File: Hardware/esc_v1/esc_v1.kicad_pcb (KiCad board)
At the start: 4 copper layers, 127 parts, among them J1 vcc_connector, J2 SWD_tag_connect, J3 motor_connector, J4 10118193-0001LF, Q1 IRFH7084TRPBF, Q2 IRFH7084TRPBF, Q3 IRFH7084TRPBF, Q4 IRFH7084TRPBF, Q5 IRFH7084TRPBF, Q6 IRFH7084TRPBF, SW1 SW_Push, U1 AZ1117CH-5.0TRG1, U10 MAX40056UAUA/V+, U2 AZ1117CH-3.3TRG1, U3 TPS5450DDAR, U4 ATSAME70J21A-AN, U5 CP2102N-Axx-xQFN24, U6 UCC27282DR, U7 UCC27282DR, U8 UCC27282DR, U9 MAX40056UAUA/V+, Y1 Crystal_GND2

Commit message: Fixing footprints
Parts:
- Q1, Q2, Q3, Q4, Q5, Q6: footprint IRFH7084PbF:IRFH7084TRPBF -> IRFH7084PbF:Infineon-PQFN5x6-G-02_2017-22-MFG
- moved Q1 56.5 mm to (207.9, 110.3)
- moved Q3 53.1 mm to (201.5, 100.6)
- moved Q6 48.5 mm to (207.9, 100.6)
- moved Q4 42.1 mm to (201.5, 110.3)
- moved Q5 38.5 mm to (183.1, 88.4)
- moved Q2 34.6 mm to (195.1, 100.6)
- moved D1 21.2 mm to (147.0, 113.5), turned to 90 degrees
- moved D4 18.0 mm to (144.0, 113.5), turned to 90 degrees
- moved R26 17.1 mm to (145.0, 113.5), turned to -90 degrees
- moved D5 15.8 mm to (141.0, 113.5), turned to 90 degrees
- moved C35 14.8 mm to (126.0, 96.0), turned to 0 degrees
- moved D13 13.8 mm to (132.0, 95.0), turned to 180 degrees
- moved C34 13.3 mm to (121.0, 103.0)
- moved C36 12.1 mm to (126.0, 94.0), turned to 0 degrees
- moved U6 11.7 mm to (125.0, 101.0)
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
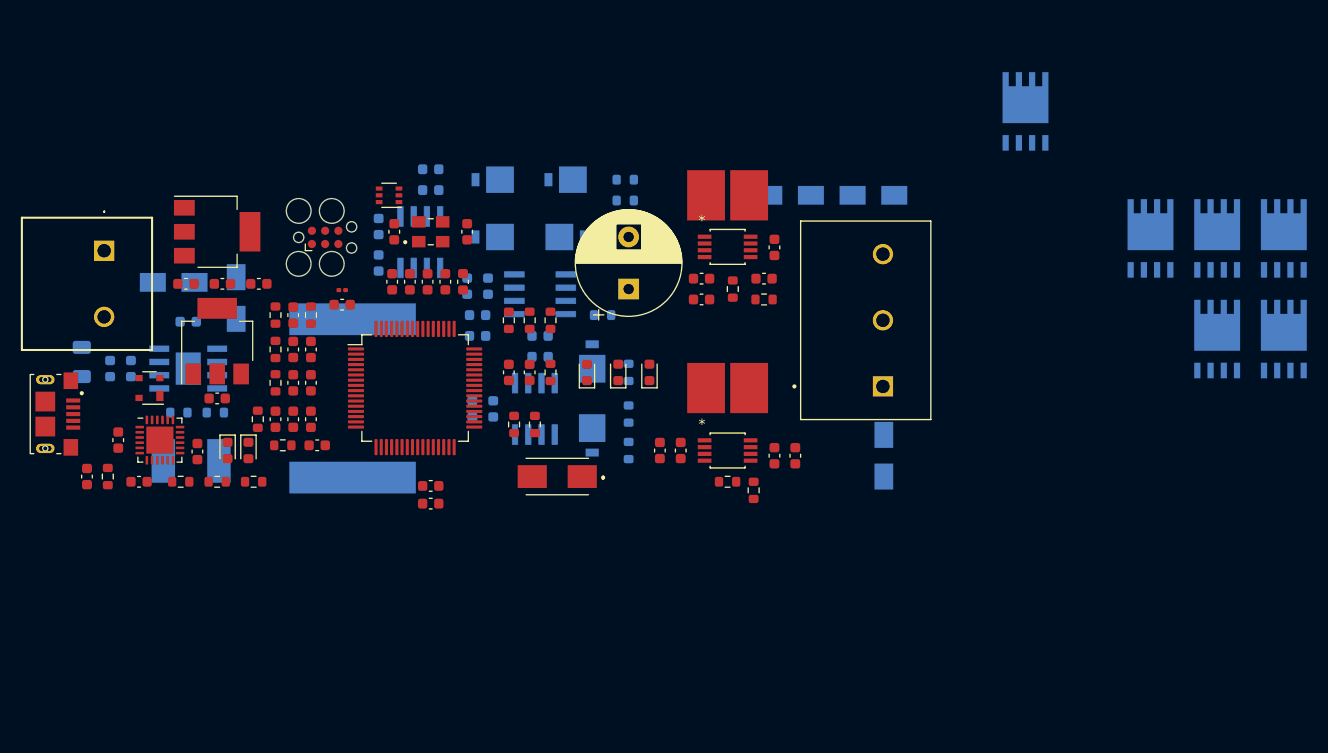
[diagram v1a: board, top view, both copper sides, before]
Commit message: changed gate driver, removed 10V buck and 5V LDO, added 5V buck. Started on Layout
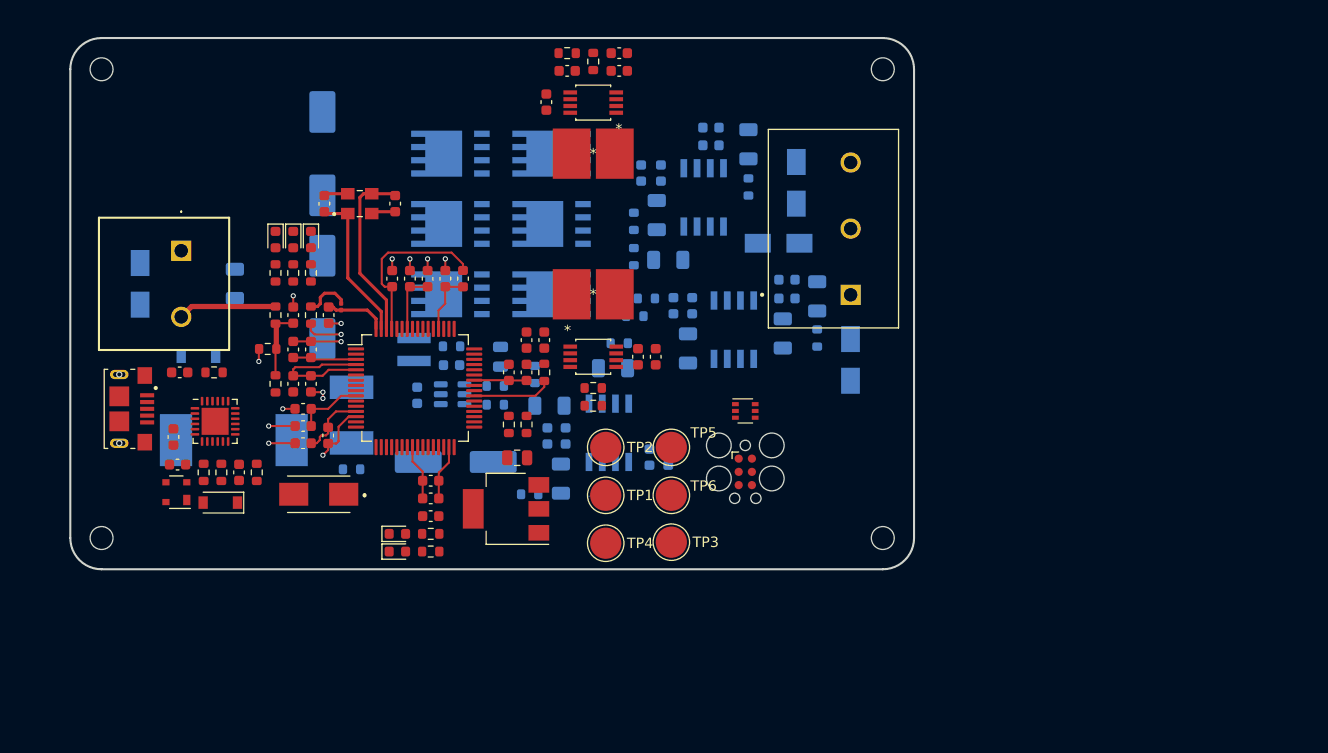
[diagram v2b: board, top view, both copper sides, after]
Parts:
- removed D11, D12: LED orange, LED_SMD:LED_0603_1608Metric
- removed R20, R21: 330R, Resistor_SMD:R_0603_1608Metric
- removed U7, U8: UCC27282DR, UCC27282DR:SOIC127P599X175-8N
- added D19: D_Schottky, Diode_SMD:D_1206_3216Metric, B.Cu at (156.5, 91.6)
- added D20: D_Schottky, Diode_SMD:D_1206_3216Metric, B.Cu at (148.8, 102.7)
- added D21: D_Schottky, Diode_SMD:D_1206_3216Metric, B.Cu at (147.7, 98.4)
- added D22: LED green, LED_SMD:LED_0603_1608Metric, F.Cu at (122.8, 129.0)
- added D23: D_Schottky, Diode_SMD:D_SOD-123, F.Cu at (105.8, 126.0)
- added D24: D_Schottky, Diode_SMD:D_SOD-123, B.Cu at (103.7, 112.0)
- added H1: MountingHole, MountingHole:MountingHole_2.2mm_M2, F.Cu at (94.4, 84.4)
- added H2: MountingHole, MountingHole:MountingHole_2.2mm_M2, F.Cu at (169.4, 129.4)
- added H3: MountingHole, MountingHole:MountingHole_2.2mm_M2, F.Cu at (94.4, 129.4)
- added H4: MountingHole, MountingHole:MountingHole_2.2mm_M2, F.Cu at (169.4, 84.4)
- added IC1: RT8259GE, Package_TO_SOT_SMD:SOT-23-6, B.Cu at (128.1, 115.6)
- added L3: 47uH, SRP1265A-470M:SRP1265A, B.Cu at (107.1, 120.0)
- added R12: 1K, Resistor_SMD:R_0603_1608Metric, F.Cu at (126.0, 129.0)
- added R34: 10R, Resistor_SMD:R_0603_1608Metric, B.Cu at (146.7, 106.4)
- added R35: 0R, Resistor_SMD:R_0603_1608Metric, B.Cu at (156.5, 95.7)
- added R36: 10R, Resistor_SMD:R_0603_1608Metric, B.Cu at (145.5, 102.4)
- added R37: 10R, Resistor_SMD:R_0603_1608Metric, B.Cu at (145.5, 99.0)
- added R5: 62K, Resistor_SMD:R_0603_1608Metric, B.Cu at (132.2, 114.8)
- added R6: 11.8K, Resistor_SMD:R_0603_1608Metric, B.Cu at (132.2, 116.6)
- added TP1: TestPoint, TestPoint:TestPoint_Pad_D3.0mm, F.Cu at (142.8, 125.3)
- added TP2: TestPoint, TestPoint:TestPoint_Pad_D3.0mm, F.Cu at (142.8, 120.7)
- added TP3: TestPoint, TestPoint:TestPoint_Pad_D3.0mm, F.Cu at (149.1, 129.8)
- added TP4: TestPoint, TestPoint:TestPoint_Pad_D3.0mm, F.Cu at (142.8, 129.9)
- added TP5: TestPoint, TestPoint:TestPoint_Pad_D3.0mm, F.Cu at (149.1, 120.7)
- added TP6: TestPoint, TestPoint:TestPoint_Pad_D3.0mm, F.Cu at (149.1, 125.3)
- C10: value 150uF, 50mOhm -> 1uF; footprint T510E107M025ATE050:T510E107M025AT E050 -> Capacitor_SMD:C_0603_1608Metric
- C2: moved to B.Cu
- C33, C37: value 1uF -> 1000pF
- C34, C38, C44: value 1000pF -> 100nF
- C35, C39: value 100nF -> 1uF
- C36, C42: value 1000pF -> 1uF
- C4: value 22uF -> 10nF
- C40: value 1000pF -> 270uF; footprint Capacitor_SMD:C_0603_1608Metric -> Capacitor_SMD:CP_Elec_10x10
- C41: value 1uF -> 270uF; footprint Capacitor_SMD:C_0603_1608Metric -> Capacitor_SMD:CP_Elec_10x10
- C43: value 100nF -> 1000pF
- C45: value 1000uF -> 1uF; footprint Capacitor_THT:CP_Radial_D10.0mm_P5.00mm -> Capacitor_SMD:C_0603_1608Metric; moved to B.Cu
- C5: value 22uF -> 100uF; footprint Capacitor_SMD:C_0603_1608Metric -> T510E107M025ATE050:T510E107M025AT E050
- C6: footprint Capacitor_SMD:C_0603_1608Metric -> Capacitor_SMD:C_0805_2012Metric; moved to B.Cu
- C7: footprint Capacitor_SMD:C_0603_1608Metric -> Capacitor_SMD:C_0805_2012Metric
- C8: value 10nF -> 390uF, 20mOhm; footprint Capacitor_SMD:C_0603_1608Metric -> Capacitor_SMD:C_Elec_8x10.2
- D10: value Schottky, 0.5V 3A -> LED green; footprint Diode_SMD:D_SMA -> LED_SMD:LED_0603_1608Metric; moved to F.Cu
- D13, D14, D15, D16, D17, D18: footprint SS2P4-M3_84A:SS2P4M384A -> Diode_SMD:D_1206_3216Metric
- L1: value 15uH, 14.4mOhm -> 10uH; footprint IHLP6767GZER150M11:INDPM172172X700N -> 744025100:Wuerth_Elektronik-744025100-Manufacturer_Recommended
- R1, R2, R3: value 330R -> 1K
- R10: value 10K -> 1K; moved to F.Cu
- R11: value 1.4K -> 0R
- R23, R26: value 1R -> 0R
- R24, R25, R27: value 1R -> 10R
- U1: value AZ1117CH-5.0TRG1 -> FAN7390MX; footprint Package_TO_SOT_SMD:SOT-223-3_TabPin2 -> FAN7390MX:Fairchild-CASE_751EG-0-0-0; moved to B.Cu
- U3: value TPS5450DDAR -> FAN7390MX; footprint Package_SO:TI_SO-PowerPAD-8 -> FAN7390MX:Fairchild-CASE_751EG-0-0-0
- U6: value UCC27282DR -> FAN7390MX; footprint UCC27282DR:SOIC127P599X175-8N -> FAN7390MX:Fairchild-CASE_751EG-0-0-0
- moved Q1 82.0 mm to (127.9, 92.5), turned to -90 degrees
- moved Q3 73.8 mm to (127.9, 106.0), turned to -90 degrees
- moved Q6 70.3 mm to (137.6, 99.2), turned to -90 degrees
- moved Q4 64.0 mm to (137.6, 106.0), turned to -90 degrees
- moved Q2 58.1 mm to (137.6, 92.5), turned to -90 degrees
- moved Q5 56.3 mm to (127.9, 99.2), turned to -90 degrees
- moved U3 52.5 mm to (155.1, 109.4)
- moved J2 46.2 mm to (156.2, 123.0), turned to -90 degrees
- moved C10 45.8 mm to (148.8, 121.6), turned to 90 degrees
- moved D2 40.0 mm to (156.2, 117.2), turned to 0 degrees
- moved U1 38.6 mm to (143.1, 119.3), turned to 0 degrees
- moved U2 38.4 mm to (133.2, 126.6), turned to 180 degrees
- moved R22 38.3 mm to (118.4, 122.8)
- moved D1 38.1 mm to (111.1, 100.8), turned to -90 degrees
- moved C33 34.1 mm to (147.0, 121.6)
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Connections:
- net Net-(C1-Pad1) renamed /shield
- net Net-(C48-Pad1) renamed /Powerstage/measurements_phase_U/Ref
- net Net-(C52-Pad1) renamed /Powerstage/measurements_phase_V/Ref
- C10 pad 1: +10V -> /+BATT_filtered
- C2 pad 1: +10V -> /+BATT_filtered
- C33 pad 1: +10V -> /+BATT_filtered
- C34 pad 1: +10V -> /Powerstage/Gate_driver_V/Bootstrap+
- C34 pad 2: GND -> /Powerstage/Gate_driver_V/HS
- C35 pad 1: /Powerstage/Gate_driver_phase_U/GD_HB -> /Powerstage/Gate_driver_V/Bootstrap+
- C35 pad 2: /Powerstage/Gate_driver_phase_U/HS -> /Powerstage/Gate_driver_V/HS
- C36 pad 1: /Powerstage/Gate_driver_phase_U/GD_HB -> /+BATT_filtered
- C36 pad 2: /Powerstage/Gate_driver_phase_U/HS -> GND
- C37 pad 1: +10V -> /+BATT_filtered
- C38 pad 1: +10V -> /Powerstage/Gate_driver_W/Bootstrap+
- C38 pad 2: GND -> /PHASE_W
- C39 pad 1: /Powerstage/Gate_driver_phase_V/GD_HB -> /Powerstage/Gate_driver_W/Bootstrap+
- C39 pad 2: /Powerstage/Gate_driver_phase_V/HS -> /PHASE_W
- C4 pad 1: VCC -> Net-(C4-Pad1)
- C4 pad 2: GND -> Net-(C4-Pad2)
- C40 pad 1: /Powerstage/Gate_driver_phase_V/GD_HB -> Net-(C40-Pad1)
- C40 pad 2: /Powerstage/Gate_driver_phase_V/HS -> GND
- C41 pad 1: +10V -> Net-(C40-Pad1)
- C42 pad 1: +10V -> /+BATT_filtered
- C43 pad 1: /Powerstage/Gate_driver_phase_W/GD_HB -> /+BATT_filtered
- C43 pad 2: /PHASE_W -> GND
- C44 pad 1: /Powerstage/Gate_driver_phase_W/GD_HB -> /Powerstage/Gate_driver_U/Bootstrap+
- C44 pad 2: /PHASE_W -> /Powerstage/Gate_driver_U/HS
- C45 pad 1: +BATT -> /Powerstage/Gate_driver_U/Bootstrap+
- C45 pad 2: GND -> /Powerstage/Gate_driver_U/HS
- C5 pad 1: VCC -> /+BATT_filtered
- C8 pad 2: Net-(C8-Pad2) -> GND
- D10 pad 1: Net-(C8-Pad2) -> GND
- D10 pad 2: GND -> Net-(D10-Pad2)
- D13 pad 1: /Powerstage/Gate_driver_phase_U/GD_HS -> /Powerstage/Gate_driver_V/Bootstrap+
- D13 pad 2: /Powerstage/Gate_driver_phase_U/HS -> Net-(D13-Pad2)
- D14 pad 1: /Powerstage/Gate_driver_phase_U/GD_LO -> /Powerstage/Gate_driver_V/GD_HO
- D14 pad 2: GND -> /Powerstage/Gate_driver_V/HS
- D15 pad 1: /Powerstage/Gate_driver_phase_V/GD_HS -> /Powerstage/Gate_driver_V/GD_LO
- D15 pad 2: /Powerstage/Gate_driver_phase_V/HS -> GND
- D16 pad 1: /Powerstage/Gate_driver_phase_V/GD_LO -> /Powerstage/Gate_driver_W/Bootstrap+
- D16 pad 2: GND -> Net-(D16-Pad2)
- D17 pad 1: /Powerstage/Gate_driver_phase_W/GD_HS -> /Powerstage/Gate_driver_W/GD_HO
- D18 pad 1: /Powerstage/Gate_driver_phase_W/GD_LO -> /Powerstage/Gate_driver_W/GD_LO
- F1 pad 2: VCC -> Net-(C40-Pad1)
- J4 pad 1: +5V -> /VBUS
- L1 pad 1: Net-(C8-Pad2) -> Net-(C4-Pad2)
- L1 pad 2: +10V -> Net-(L1-Pad2)
- Q1 pad 1: /Powerstage/Gate_driver_phase_U/HS -> /Powerstage/Gate_driver_U/HS
- Q1 pad 2: /Powerstage/Gate_driver_phase_U/HS -> /Powerstage/Gate_driver_U/HS
- Q1 pad 3: /Powerstage/Gate_driver_phase_U/HS -> /Powerstage/Gate_driver_U/HS
- Q1 pad 4: /Powerstage/Gate_driver_phase_U/HO -> /Powerstage/Gate_driver_U/HO
- Q1 pad 5-6-7-8: +BATT -> Net-(C40-Pad1)
- Q2 pad 4: /Powerstage/Gate_driver_phase_U/LO -> /Powerstage/Gate_driver_U/LO
- Q2 pad 5-6-7-8: /Powerstage/Gate_driver_phase_U/HS -> /Powerstage/Gate_driver_U/HS
- Q3 pad 1: /Powerstage/Gate_driver_phase_V/HS -> /Powerstage/Gate_driver_V/HS
- Q3 pad 2: /Powerstage/Gate_driver_phase_V/HS -> /Powerstage/Gate_driver_V/HS
- Q3 pad 3: /Powerstage/Gate_driver_phase_V/HS -> /Powerstage/Gate_driver_V/HS
- Q3 pad 4: /Powerstage/Gate_driver_phase_V/HO -> /Powerstage/Gate_driver_V/HO
- Q3 pad 5-6-7-8: +BATT -> Net-(C40-Pad1)
- Q4 pad 4: /Powerstage/Gate_driver_phase_V/LO -> /Powerstage/Gate_driver_V/LO
- Q4 pad 5-6-7-8: /Powerstage/Gate_driver_phase_V/HS -> /Powerstage/Gate_driver_V/HS
- Q5 pad 4: /Powerstage/Gate_driver_phase_W/HO -> /Powerstage/Gate_driver_W/HO
- Q5 pad 5-6-7-8: +BATT -> Net-(C40-Pad1)
- Q6 pad 4: /Powerstage/Gate_driver_phase_W/LO -> /Powerstage/Gate_driver_W/LO
- R10 pad 1: +10V -> +3V3
- R10 pad 2: Net-(R10-Pad2) -> Net-(D10-Pad2)
- R11 pad 1: Net-(R10-Pad2) -> Net-(L1-Pad2)
- R11 pad 2: GND -> +5V
- R22 pad 1: /Powerstage/Gate_driver_phase_U/GD_HS -> /+BATT_filtered
- R22 pad 2: /Powerstage/Gate_driver_phase_U/HO -> Net-(C8-Pad1)
- R23 pad 1: /Powerstage/Gate_driver_phase_U/GD_LO -> Net-(D13-Pad2)
- R23 pad 2: /Powerstage/Gate_driver_phase_U/LO -> /+BATT_filtered
- R24 pad 1: /Powerstage/Gate_driver_phase_V/GD_HS -> /Powerstage/Gate_driver_V/HO
- R24 pad 2: /Powerstage/Gate_driver_phase_V/HO -> /Powerstage/Gate_driver_V/GD_HO
- R25 pad 1: /Powerstage/Gate_driver_phase_V/GD_LO -> /Powerstage/Gate_driver_V/LO
- R25 pad 2: /Powerstage/Gate_driver_phase_V/LO -> /Powerstage/Gate_driver_V/GD_LO
- R26 pad 1: /Powerstage/Gate_driver_phase_W/GD_HS -> Net-(D16-Pad2)
- R26 pad 2: /Powerstage/Gate_driver_phase_W/HO -> /+BATT_filtered
- R27 pad 1: /Powerstage/Gate_driver_phase_W/GD_LO -> /Powerstage/Gate_driver_W/HO
- R27 pad 2: /Powerstage/Gate_driver_phase_W/LO -> /Powerstage/Gate_driver_W/GD_HO
- R28 pad 1: /Powerstage/Gate_driver_phase_U/HS -> /Powerstage/Gate_driver_U/HS
- R31 pad 1: /Powerstage/Gate_driver_phase_V/HS -> /Powerstage/Gate_driver_V/HS
- R7 pad 1: VCC -> +BATT
- U1 pad 1: GND -> /MCU/PWM_H1
- U1 pad 2: +5V -> /MCU/PWM_L1
- U1 pad 3: +10V -> GND
- U10 pad 1: /Powerstage/Gate_driver_phase_V/HS -> /Powerstage/Gate_driver_V/HS
- U3 pad 1: Net-(C8-Pad1) -> /MCU/PWM_H2
- U3 pad 2: unconnected-(U3-Pad2) -> /MCU/PWM_L2
- U3 pad 3: unconnected-(U3-Pad3) -> GND
- U3 pad 4: Net-(R10-Pad2) -> /Powerstage/Gate_driver_W/GD_LO
- U3 pad 5: unconnected-(U3-Pad5) -> /+BATT_filtered
- U3 pad 6: GND -> /PHASE_W
- U3 pad 7: VCC -> /Powerstage/Gate_driver_W/GD_HO
- U3 pad 8: Net-(C8-Pad2) -> /Powerstage/Gate_driver_W/Bootstrap+
- U5 pad 13: Net-(D12-Pad1) -> unconnected-(U5-Pad13)
- U5 pad 14: Net-(D11-Pad1) -> unconnected-(U5-Pad14)
- U6 pad 1: +10V -> /MCU/PWM_H0
- U6 pad 2: /Powerstage/Gate_driver_phase_U/GD_HB -> /MCU/PWM_L0
- U6 pad 3: /Powerstage/Gate_driver_phase_U/GD_HS -> GND
- U6 pad 4: /Powerstage/Gate_driver_phase_U/HS -> /Powerstage/Gate_driver_U/GD_LO
- U6 pad 5: /MCU/PWM_H0 -> /+BATT_filtered
- U6 pad 6: /MCU/PWM_L0 -> /Powerstage/Gate_driver_U/HS
- U6 pad 7: GND -> /Powerstage/Gate_driver_U/GD_HO
- U6 pad 8: /Powerstage/Gate_driver_phase_U/GD_LO -> /Powerstage/Gate_driver_U/Bootstrap+
- U9 pad 1: /Powerstage/Gate_driver_phase_U/HS -> /Powerstage/Gate_driver_U/HS
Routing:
- net GND: track 0.00 -> 36.4 mm, vias 0 -> 14
- net /MCU/VDDCORE: track 0.00 -> 34.7 mm
- net +3V3: track 0.00 -> 34.2 mm, vias 0 -> 1
- net /MCU/XOUT: track 0.00 -> 17.6 mm
- net /MCU/XIN: track 0.00 -> 14.7 mm
- net +BATT: track 0.00 -> 9.46 mm
- net /SWCLK: track 0.00 -> 7.65 mm
- net Net-(C9-Pad1): track 0.00 -> 6.73 mm
- net /MCU/VDDPLL: track 0.00 -> 6.02 mm
- net /MCU/VDDPLLUSB: track 0.00 -> 5.99 mm
- net Net-(L2-Pad1): track 0.00 -> 4.41 mm
- net /PHASE_W: track 0.00 -> 0.78 mm
- net /Powerstage/Gate_driver_V/GD_HO: track 0.00 -> 0.55 mm
- added copper zone on In1.Cu, net +3V3
- added copper zone on In2.Cu, net GND
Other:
- board outline added: 81 x 51 mm

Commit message: Continued on layout
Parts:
- moved H2 35.5 mm to (119.9, 140.8)
- moved H0 34.3 mm to (112.7, 141.7)
- moved L0 34.3 mm to (112.7, 137.1)
- moved L1 34.3 mm to (112.7, 146.2)
- moved H1 34.3 mm to (119.0, 146.2)
- moved L2 27.3 mm to (126.4, 140.4)
- moved D10 22.1 mm to (144.8, 128.2), turned to 90 degrees
- moved R30 20.5 mm to (122.8, 91.9), turned to 90 degrees
- moved R29 20.4 mm to (122.8, 95.2), turned to 90 degrees
- moved D22 20.0 mm to (142.8, 128.2), turned to 90 degrees
- moved R10 19.6 mm to (144.8, 125.0), turned to -90 degrees
- moved C46 17.8 mm to (128.8, 91.9), turned to -90 degrees
- moved C48 17.5 mm to (125.8, 96.0)
- moved R12 17.2 mm to (142.8, 125.0), turned to -90 degrees
- moved U9 16.3 mm to (125.9, 91.9), turned to -90 degrees
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- renumbered TP1 to H0, TP3 to H1, TP5 to H2, TP2 to L0, TP4 to L1, TP6 to L2
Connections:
- D9 pad 2: +5V -> /VBUS
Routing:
- net GND: track 36.4 -> 125.0 mm, vias 14 -> 35
- net +5V: track 0.00 -> 80.2 mm, vias 0 -> 2
- net /+BATT_filtered: track 0.00 -> 50.4 mm
- net +3V3: track 34.2 -> 75.9 mm, vias 1 -> 14
- net /NRST: track 0.00 -> 41.2 mm, vias 0 -> 2
- net /MCU/LED_2: track 0.00 -> 36.5 mm, vias 0 -> 2
- net /MCU/LED_1: track 0.00 -> 34.6 mm, vias 0 -> 2
- net /Powerstage/Gate_driver_W/GD_HO: track 0.00 -> 33.7 mm
- net /TRACESWO: track 0.00 -> 33.5 mm, vias 0 -> 3
- net /MCU/LED_0: track 0.00 -> 32.7 mm, vias 0 -> 2
- net /SWDIO: track 0.11 -> 32.1 mm
- net /Powerstage/Gate_driver_U/HS: track 0.00 -> 31.8 mm, vias 0 -> 6
- net /PHASE_W: track 0.78 -> 25.8 mm, vias 0 -> 6
- net /SWCLK: track 7.65 -> 30.7 mm
- net /MCU/UART0_TX: track 0.00 -> 21.3 mm
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- added copper zone on F.Cu, net +3V3
- added copper zone on In1.Cu, net +5V
- added copper zone on B.Cu, net +BATT
- added copper zone on F.Cu, net /PHASE_U
- added copper zone on F.Cu, net /PHASE_V
- added copper zone on B.Cu, net /PHASE_W
- added copper zone on F.Cu, net /PHASE_W
- added copper zone on B.Cu, net /Powerstage/Gate_driver_U/HS
- added copper zone on F.Cu, net /Powerstage/Gate_driver_U/HS
- added copper zone on B.Cu, net /Powerstage/Gate_driver_V/HS
- added copper zone on F.Cu, net /Powerstage/Gate_driver_V/HS
- added copper zone on B.Cu, net GND
- added copper zone on B.Cu, net Net-(C40-Pad1)
- added copper zone on B.Cu, net Net-(D24-Pad1)
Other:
- board size 81 x 51 mm -> 81 x 45 mm

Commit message: Continued on layout
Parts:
- H0, H1, H2, L0, L1, L2: footprint TestPoint:TestPoint_Pad_D3.0mm -> TestPoint:TestPoint_Pad_D2.0mm
- moved H0 57.2 mm to (153.9, 102.1), turned to 180 degrees
- moved L0 51.6 mm to (150.6, 102.0), turned to 180 degrees
- moved H2 41.2 mm to (151.7, 114.6)
- moved L1 37.1 mm to (138.2, 119.3)
- moved L2 33.8 mm to (148.3, 114.7)
- moved H1 33.1 mm to (141.1, 121.6)
- moved C2 10.9 mm to (125.1, 126.4), turned to -90 degrees
- moved R6 9.65 mm to (131.9, 126.2), turned to -90 degrees
- moved R22 9.19 mm to (122.7, 114.7), turned to 90 degrees
- moved R5 9.04 mm to (131.9, 123.1)
- moved R11 8.89 mm to (131.6, 120.0)
- moved C4 8.86 mm to (128.6, 121.7)
- moved C6 8.86 mm to (133.9, 122.7)
- moved IC1 8.86 mm to (128.6, 124.5)
- moved L1 8.65 mm to (124.1, 121.1)
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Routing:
- net /MCU/PWM_L2: track 0.00 -> 44.9 mm, vias 0 -> 3
- net /MCU/PWM_H2: track 0.00 -> 35.2 mm, vias 0 -> 3
- net +5V: track 80.2 -> 50.7 mm, vias 2 -> 4
- net /+BATT_filtered: track 50.4 -> 79.8 mm, vias 0 -> 1
- net /MCU/PWM_H1: track 0.00 -> 26.8 mm, vias 0 -> 3
- net /Powerstage/Gate_driver_U/HO: track 0.00 -> 21.8 mm, vias 0 -> 2
- net /MCU/PWM_L1: track 0.00 -> 20.6 mm, vias 0 -> 3
- net /Powerstage/Gate_driver_W/HO: track 0.00 -> 20.1 mm, vias 0 -> 2
- net Net-(L1-Pad2): track 2.13 -> 9.89 mm
- net /Powerstage/Gate_driver_W/GD_HO: track 33.7 -> 28.8 mm
- net /SWDIO: track 32.1 -> 35.4 mm
- net Net-(D13-Pad2): track 2.22 -> 0.01 mm
- net Net-(C8-Pad1): track 5.86 -> 3.89 mm
- net GND: track 125.0 -> 123.8 mm
- net /MCU/LED_2: track 36.5 -> 37.7 mm
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- added copper zone on B.Cu, net +5V
- added copper zone on F.Cu, net +5V
- added copper zone on B.Cu, net /+BATT_filtered
- removed copper zone on In1.Cu, net +5V

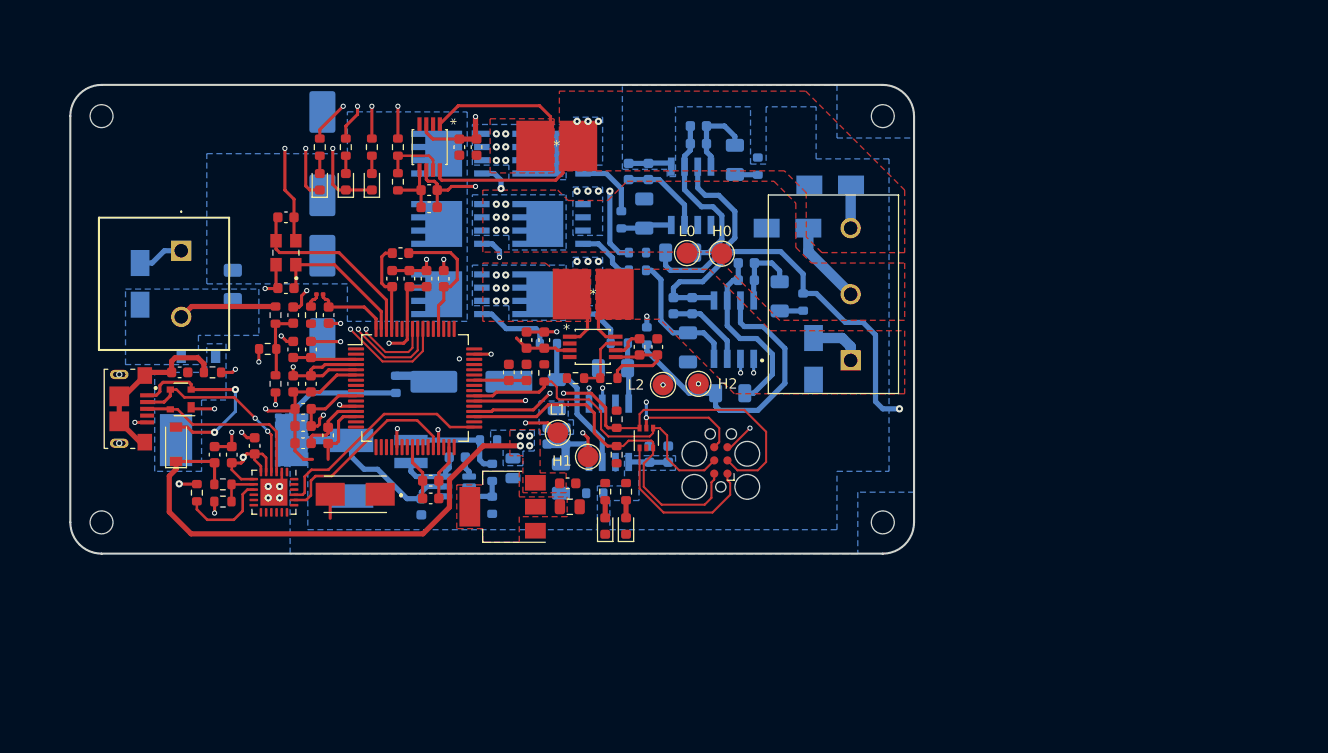
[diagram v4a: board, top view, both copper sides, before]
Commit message: Changed to 6 layer pcb, increased space by 10mm, redid gate driver traces and power planes
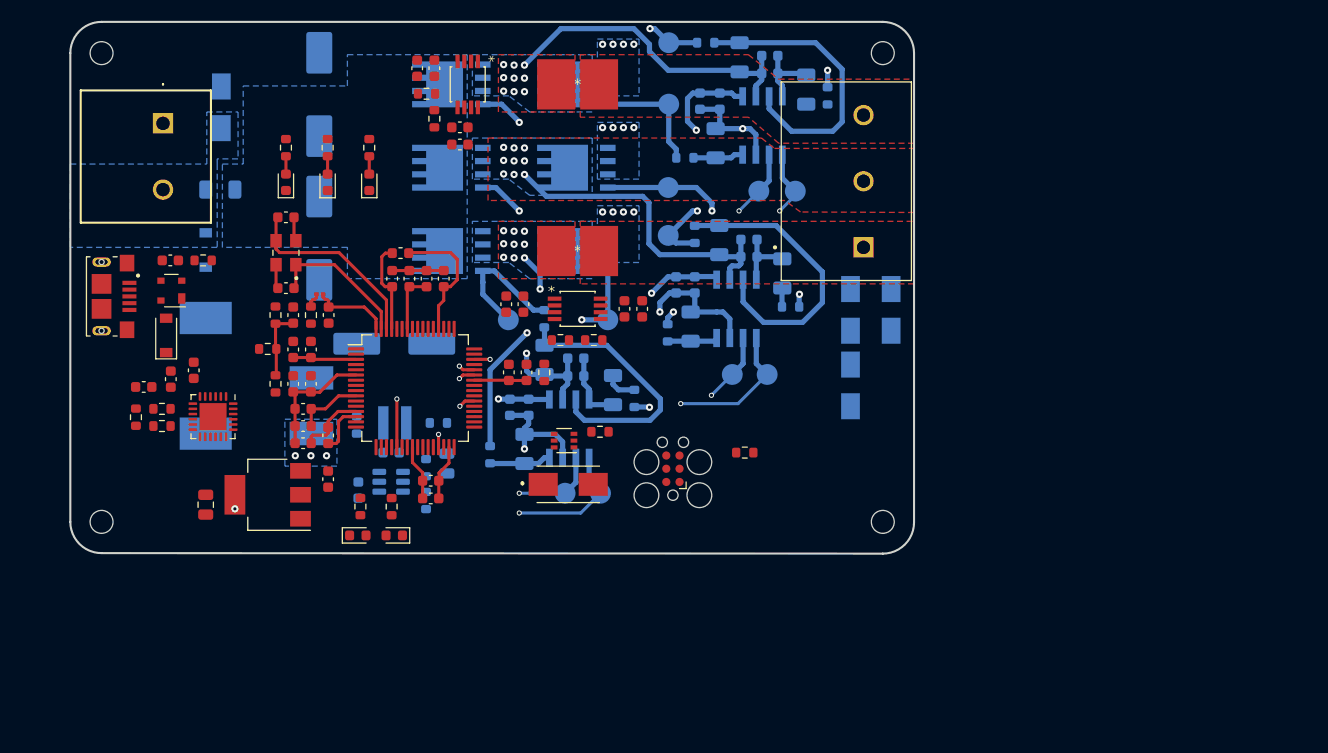
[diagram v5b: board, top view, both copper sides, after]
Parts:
- added HO_U: TestPoint, TestPoint:TestPoint_Pad_D2.0mm, B.Cu at (148.8, 81.8)
- added HO_V: TestPoint, TestPoint:TestPoint_Pad_D2.0mm, B.Cu at (133.4, 108.5)
- added HO_W: TestPoint, TestPoint:TestPoint_Pad_D2.0mm, B.Cu at (148.8, 100.3)
- added LO_U: TestPoint, TestPoint:TestPoint_Pad_D2.0mm, B.Cu at (148.8, 87.8)
- added LO_W: TestPoint, TestPoint:TestPoint_Pad_D2.0mm, B.Cu at (148.8, 95.8)
- added LO_W: TestPoint, TestPoint:TestPoint_Pad_D2.0mm, B.Cu at (143.0, 108.5)
- H0, H1, H2, L0, L1, L2: moved to B.Cu
- moved C7 35.0 mm to (104.4, 126.2), turned to -90 degrees
- moved D10 25.8 mm to (119.0, 129.2), turned to 0 degrees
- moved R10 25.5 mm to (119.2, 126.4)
- moved C3 23.0 mm to (116.2, 123.8), turned to -90 degrees
- moved U2 22.6 mm to (110.3, 125.2)
- moved R36 21.2 mm to (152.4, 81.8)
- moved R12 20.6 mm to (122.2, 126.4)
- moved D22 20.3 mm to (122.5, 129.2), turned to 180 degrees
- moved SW1 19.8 mm to (138.8, 124.2), turned to 0 degrees
- moved D20 19.6 mm to (155.7, 83.2), turned to -90 degrees
- moved D3 18.7 mm to (105.9, 88.0)
- moved R25 16.4 mm to (131.7, 121.4), turned to -90 degrees
- moved C10 15.9 mm to (133.6, 116.8), turned to -90 degrees
- moved D17 14.7 mm to (153.7, 100.8), turned to -90 degrees
- moved D8 13.3 mm to (170.2, 107.5), turned to -90 degrees
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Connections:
- U4 pad 7: /MCU/overcurr_err_U -> /MCU/overcurr_err_V
- U4 pad 8: /MCU/overcurr_err_V -> /MCU/overcurr_err_U
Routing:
- net +3V3: track 77.0 -> 17.6 mm, vias 6 -> 1
- net GND: track 123.8 -> 65.4 mm, vias 35 -> 15
- net /+BATT_filtered: track 79.8 -> 25.4 mm, vias 1 -> 9
- net +5V: track 50.7 -> 0.00 mm, vias 4 -> 0
- net /MCU/PWM_H0: track 0.00 -> 47.8 mm, vias 0 -> 2
- net /MCU/PWM_L0: track 0.00 -> 44.6 mm, vias 0 -> 2
- net /NRST: track 40.9 -> 0.00 mm, vias 2 -> 0
- net /MCU/LED_2: track 37.7 -> 0.00 mm, vias 2 -> 0
- net /SWDIO: track 35.4 -> 0.11 mm
- net /MCU/LED_1: track 34.6 -> 0.00 mm, vias 2 -> 0
- net /TRACESWO: track 33.0 -> 0.00 mm, vias 3 -> 0
- net /MCU/LED_0: track 32.7 -> 0.00 mm, vias 2 -> 0
- net /SWCLK: track 31.7 -> 0.00 mm
- net /MCU/UART0_TX: track 21.9 -> 0.00 mm
- net /Powerstage/Gate_driver_V/LO: track 4.59 -> 25.4 mm, vias 0 -> 2
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- added copper zone on In2.Cu, net +3V3
- added copper zone on In2.Cu, net /+BATT_filtered
- added copper zone on In1.Cu, net GND
- added copper zone on In4.Cu, net GND
- removed copper zone on F.Cu, net +3V3
- removed copper zone on In1.Cu, net +3V3
- removed copper zone on B.Cu, net +5V
- removed copper zone on F.Cu, net +5V
- removed copper zone on In2.Cu, net GND
- removed copper zone on B.Cu, net Net-(D24-Pad1)
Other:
- board size 81 x 45 mm -> 81 x 51.1 mm
- copper layers 4 -> 6
